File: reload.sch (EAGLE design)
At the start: 19 parts, among them IC3 OPAMP-DUALU, Q1 BTS117

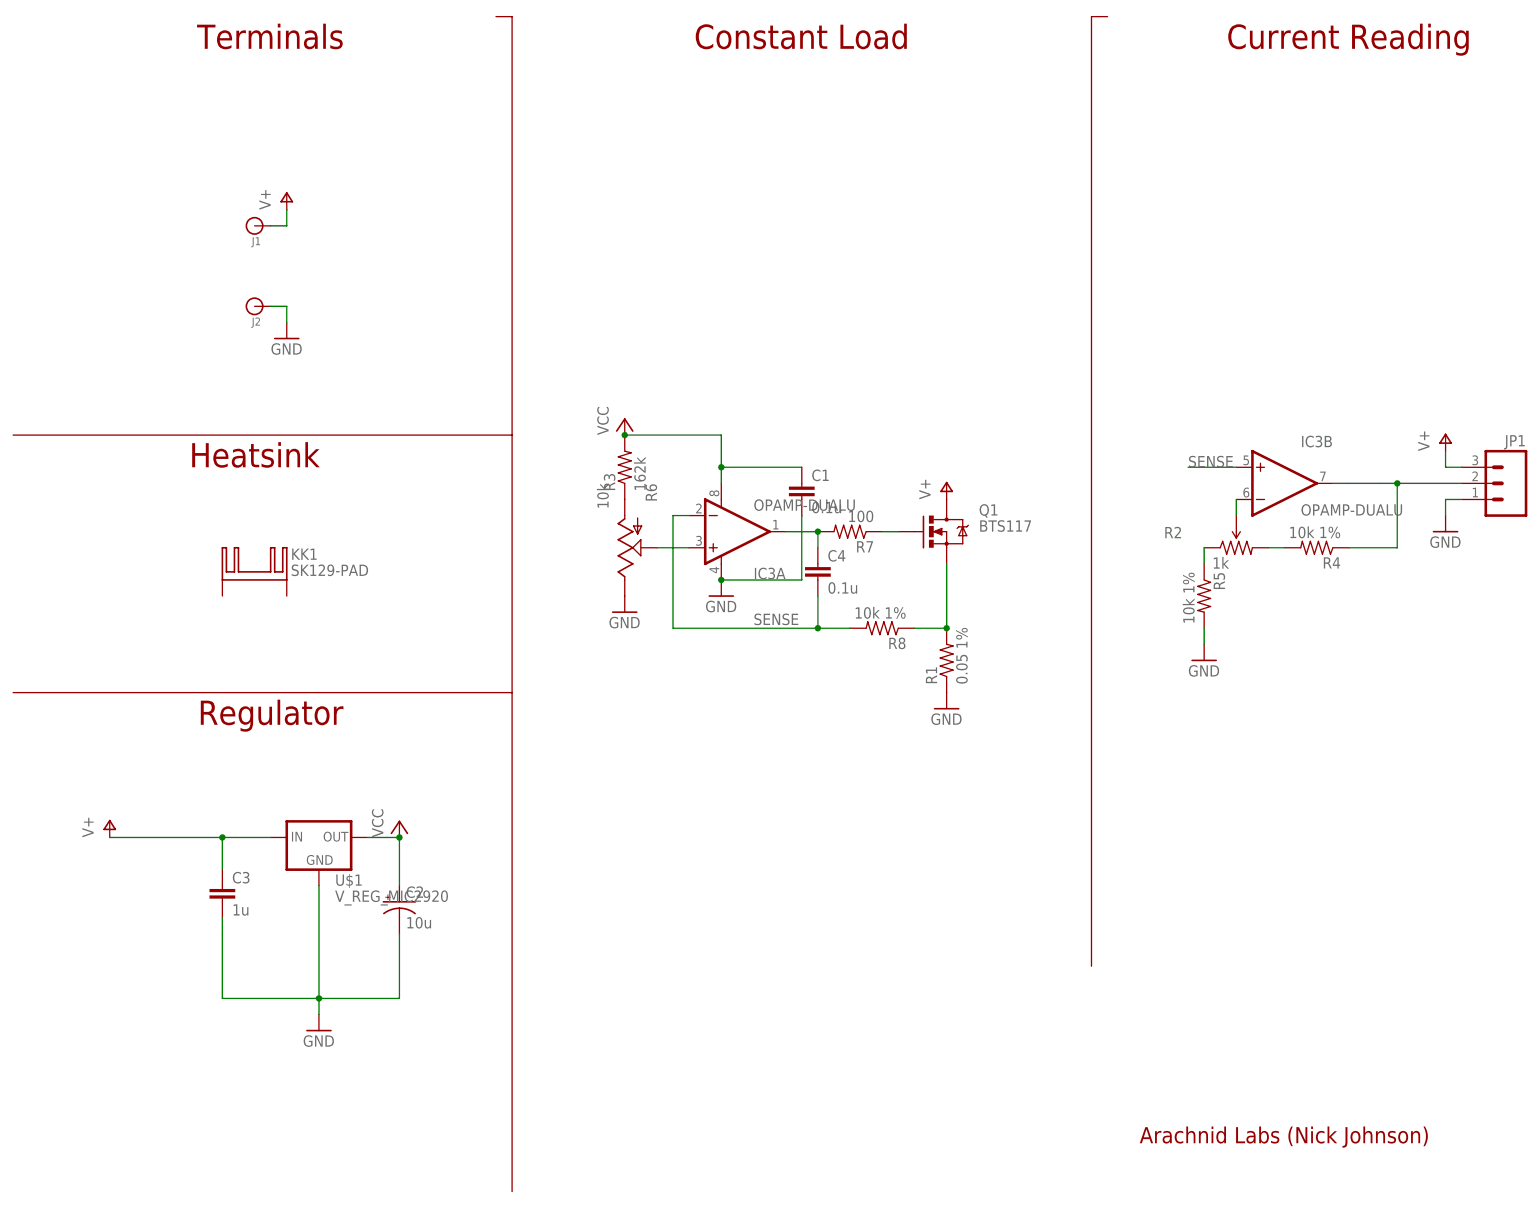
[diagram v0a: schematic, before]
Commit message: Respin with SMD parts
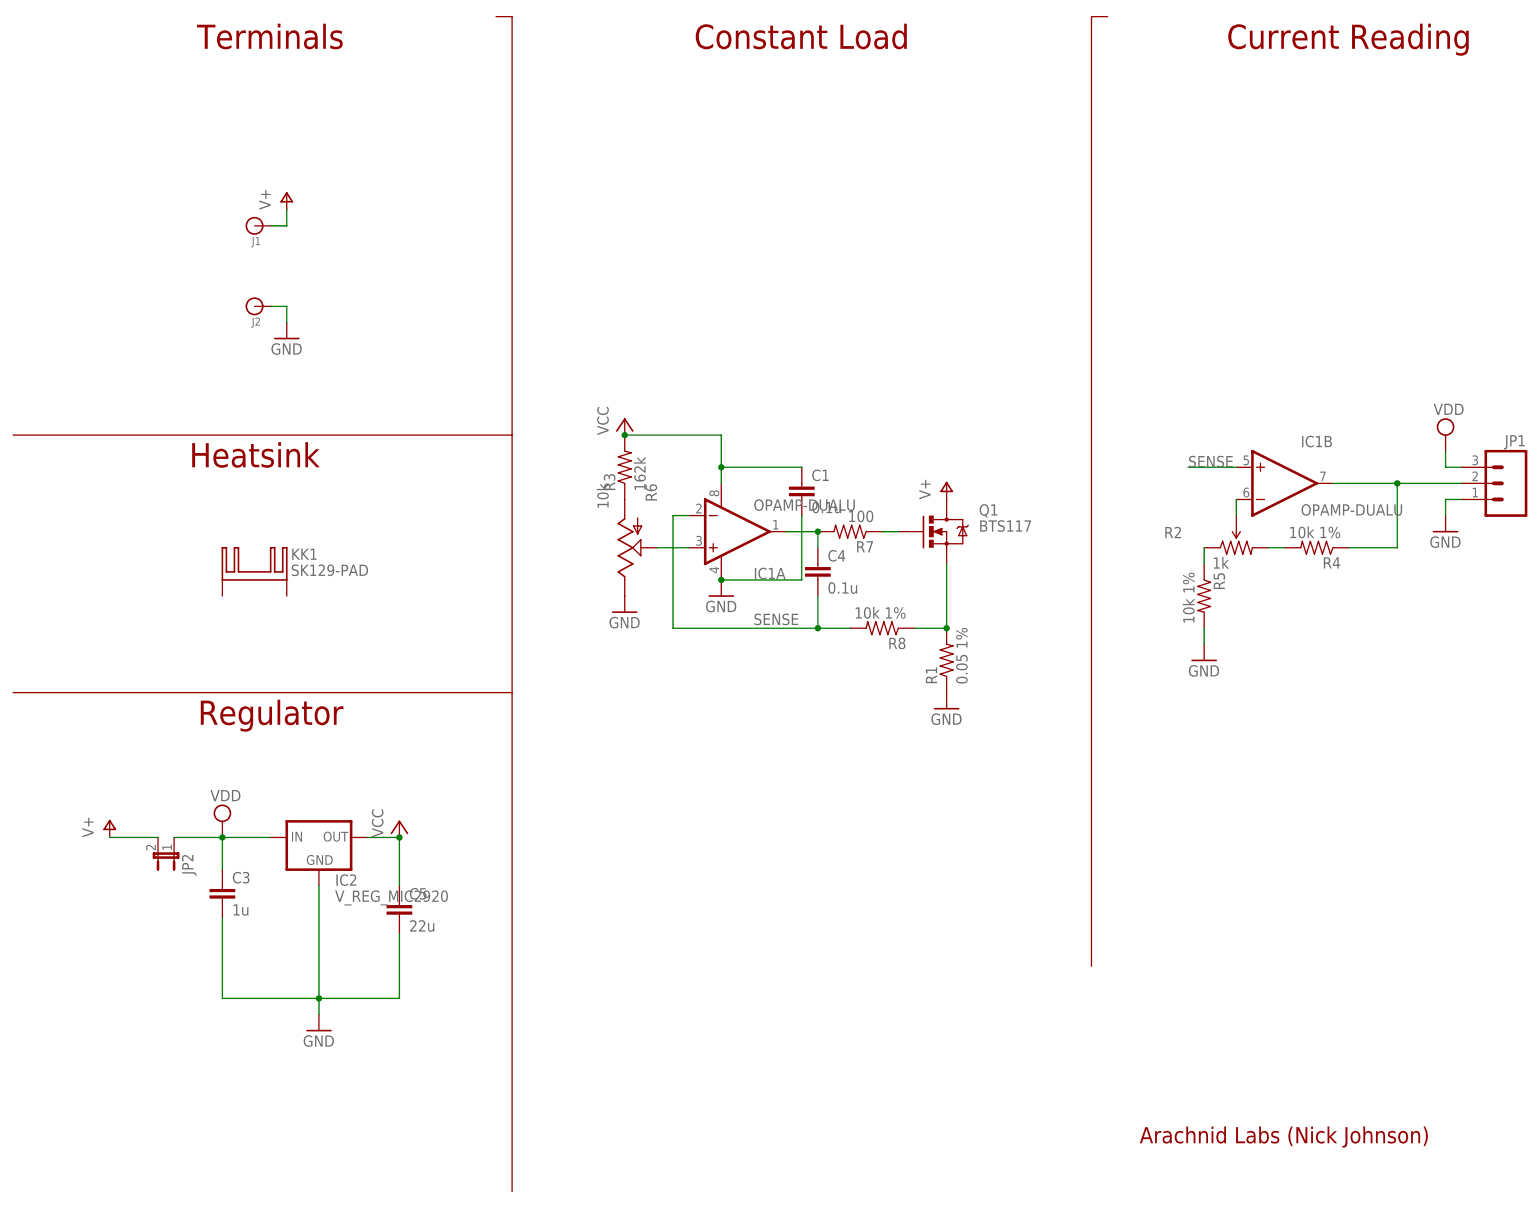
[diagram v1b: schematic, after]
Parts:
- removed C2: 10u, SparkFun-Passives:CAP_POLC
- added C5: 22u, SparkFun-Passives:CAP0805
- added JP2: (no value), SparkFun-Passives:JUMPER-2SMD-NC
- renumbered IC3 to IC1, U$1 to IC2
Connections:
- new net VDD: C3.1, IC2.IN, JP1.3, JP2.1
- net GND: now also C5.2; no longer C2.-
- net V+: now also JP2.2; no longer C3.1, IC2.IN, JP1.3
- net VCC: now also C5.1; no longer C2.+
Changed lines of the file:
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@@
 <?xml version="1.0" encoding="utf-8"?>
 <!DOCTYPE eagle SYSTEM "eagle.dtd">
-<eagle version="6.2">
+<eagle version="6.4">
 <drawing>
 <settings>
@@
 <part name="P+4" library="supply1" deviceset="V+" device=""/>
 <part name="GND7" library="supply1" deviceset="GND" device=""/>
-<part name="C2" library="SparkFun-Passives" deviceset="CAP_POL" device="C" value="10u"/>
 <part name="C3" library="SparkFun-Passives" deviceset="CAP" device="0805" value="1u"/>
 <part name="KK1" library="nickparts" deviceset="SK129-PAD" device=""/>
@@
 <part name="P+5" library="supply1" deviceset="VCC" device=""/>
 <part name="RELOAD" library="SparkFun-Aesthetics" deviceset="FRAME-LETTER" device=""/>
-<part name="IC3" library="SparkFun-AnalogIC" deviceset="OPAMP-DUAL" device="U"/>
-<part name="U$1" library="SparkFun-PowerIC" deviceset="V_REG_MIC2920" device=""/>
+<part name="IC1" library="SparkFun-AnalogIC" deviceset="OPAMP-DUAL" device="U"/>
+<part name="IC2" library="SparkFun-PowerIC" deviceset="V_REG_MIC2920" device=""/>
 <part name="JP1" library="SparkFun-Connectors" deviceset="M03" device="1X03_NO_SILK"/>
 <part name="R8" library="SparkFun-Passives" deviceset="RESISTOR" device="0805-RES" value="10k 1%"/>
 <part name="C4" library="SparkFun-Passives" deviceset="CAP" device="0805" value="0.1u"/>
-<part name="P+6" library="supply1" deviceset="V+" device=""/>
+<part name="JP2" library="SparkFun-Passives" deviceset="JUMPER-2" device="SMD-NC"/>
+<part name="SUPPLY1" library="supply2" deviceset="VDD" device=""/>
+<part name="SUPPLY2" library="supply2" deviceset="VDD" device=""/>
+<part name="C5" library="SparkFun-Passives" deviceset="CAP" device="0805" value="22u"/>
 </parts>
 <sheets>
@@
 <instance part="P+4" gate="1" x="43.18" y="157.48"/>
 <instance part="GND7" gate="1" x="43.18" y="134.62"/>
-<instance part="C2" gate="G$1" x="60.96" y="45.72"/>
 <instance part="C3" gate="G$1" x="33.02" y="45.72"/>
 <instance part="KK1" gate="G$1" x="38.1" y="96.52"/>
@@
 <instance part="RELOAD" gate="G$1" x="0" y="0"/>
 <instance part="RELOAD" gate="G$2" x="147.32" y="0"/>
-<instance part="IC3" gate="A" x="111.76" y="104.14"/>
-<instance part="IC3" gate="B" x="200.66" y="111.76"/>
-<instance part="U$1" gate="G$1" x="48.26" y="55.88"/>
+<instance part="IC1" gate="A" x="111.76" y="104.14"/>
+<instance part="IC1" gate="B" x="200.66" y="111.76"/>
+<instance part="IC2" gate="G$1" x="48.26" y="55.88"/>
 <instance part="JP1" gate="G$1" x="236.22" y="111.76" rot="MR0"/>
 <instance part="R8" gate="G$1" x="137.16" y="88.9" rot="R180"/>
 <instance part="C4" gate="G$1" x="127" y="96.52"/>
-<instance part="P+6" gate="1" x="226.06" y="119.38"/>
+<instance part="JP2" gate="A" x="25.4" y="53.34" rot="R180"/>
+<instance part="SUPPLY1" gate="G$1" x="33.02" y="58.42"/>
+<instance part="SUPPLY2" gate="G$1" x="226.06" y="119.38"/>
+<instance part="C5" gate="G$1" x="60.96" y="43.18"/>
 </instances>
 <busses>
@@
 </segment>
 <segment>
+<pinref part="JP2" gate="A" pin="2"/>
 <pinref part="P+3" gate="1" pin="V+"/>
-<wire x1="15.24" y1="55.88" x2="20.32" y2="55.88" width="0.1524" layer="91"/>
-<wire x1="25.4" y1="55.88" x2="27.94" y2="55.88" width="0.1524" layer="91"/>
-<wire x1="27.94" y1="55.88" x2="33.02" y2="55.88" width="0.1524" layer="91"/>
-<pinref part="C3" gate="G$1" pin="1"/>
-<wire x1="33.02" y1="55.88" x2="40.64" y2="55.88" width="0.1524" layer="91"/>
-<wire x1="33.02" y1="50.8" x2="33.02" y2="55.88" width="0.1524" layer="91"/>
-<junction x="33.02" y="55.88"/>
-<pinref part="U$1" gate="G$1" pin="IN"/>
-<wire x1="20.32" y1="55.88" x2="25.4" y2="55.88" width="0.1524" layer="91"/>
-</segment>
-<segment>
-<pinref part="JP1" gate="G$1" pin="3"/>
-<wire x1="228.6" y1="114.3" x2="226.06" y2="114.3" width="0.1524" layer="91"/>
-<wire x1="226.06" y1="114.3" x2="226.06" y2="116.84" width="0.1524" layer="91"/>
-<pinref part="P+6" gate="1" pin="V+"/>
+<wire x1="15.24" y1="55.88" x2="22.86" y2="55.88" width="0.1524" layer="91"/>
 </segment>
 </net>
@@
 <wire x1="193.04" y1="114.3" x2="185.42" y2="114.3" width="0.1524" layer="91"/>
 <label x="185.42" y="114.3" size="1.778" layer="95"/>
-<pinref part="IC3" gate="B" pin="+IN"/>
+<pinref part="IC1" gate="B" pin="+IN"/>
 </segment>
 <segment>
@@
 <wire x1="127" y1="88.9" x2="104.14" y2="88.9" width="0.1524" layer="91"/>
 <wire x1="104.14" y1="88.9" x2="104.14" y2="106.68" width="0.1524" layer="91"/>
-<pinref part="IC3" gate="A" pin="-IN"/>
+<pinref part="IC1" gate="A" pin="-IN"/>
 <wire x1="104.14" y1="106.68" x2="106.68" y2="106.68" width="0.1524" layer="91"/>
 <pinref part="C4" gate="G$1" pin="2"/>
@@
 <wire x1="124.46" y1="106.68" x2="124.46" y2="96.52" width="0.1524" layer="91"/>
 <wire x1="124.46" y1="96.52" x2="111.76" y2="96.52" width="0.1524" layer="91"/>
-<pinref part="IC3" gate="A" pin="V-"/>
+<pinref part="IC1" gate="A" pin="V-"/>
 <junction x="111.76" y="96.52"/>
 </segment>
@@
 <pinref part="GND4" gate="1" pin="GND"/>
 <wire x1="48.26" y1="27.94" x2="48.26" y2="30.48" width="0.1524" layer="91"/>
-<pinref part="C2" gate="G$1" pin="-"/>
 <wire x1="60.96" y1="40.64" x2="60.96" y2="30.48" width="0.1524" layer="91"/>
 <wire x1="60.96" y1="30.48" x2="48.26" y2="30.48" width="0.1524" layer="91"/>
 <wire x1="48.26" y1="30.48" x2="33.02" y2="30.48" width="0.1524" layer="91"/>
-<wire x1="33.02" y1="30.48" x2="33.02" y2="40.64" width="0.1524" layer="91"/>
+<wire x1="33.02" y1="30.48" x2="33.02" y2="43.18" width="0.1524" layer="91"/>
 <junction x="48.26" y="30.48"/>
 <pinref part="C3" gate="G$1" pin="2"/>
-<wire x1="33.02" y1="40.64" x2="33.02" y2="43.18" width="0.1524" layer="91"/>
 <wire x1="48.26" y1="48.26" x2="48.26" y2="30.48" width="0.1524" layer="91"/>
-<pinref part="U$1" gate="G$1" pin="GND"/>
+<pinref part="IC2" gate="G$1" pin="GND"/>
+<pinref part="C5" gate="G$1" pin="2"/>
 </segment>
 <segment>
@@
 <pinref part="R6" gate="G$1" pin="S"/>
 <wire x1="101.6" y1="101.6" x2="106.68" y2="101.6" width="0.1524" layer="91"/>
-<pinref part="IC3" gate="A" pin="+IN"/>
+<pinref part="IC1" gate="A" pin="+IN"/>
 </segment>
 </net>
@@
 <pinref part="R4" gate="G$1" pin="1"/>
 <wire x1="210.82" y1="101.6" x2="218.44" y2="101.6" width="0.1524" layer="91"/>
-<pinref part="IC3" gate="B" pin="OUT"/>
+<pinref part="IC1" gate="B" pin="OUT"/>
 <pinref part="JP1" gate="G$1" pin="2"/>
 <wire x1="228.6" y1="111.76" x2="218.44" y2="111.76" width="0.1524" layer="91"/>
@@
 <pinref part="R2" gate="R?" pin="WIPER"/>
 <wire x1="193.04" y1="109.22" x2="193.04" y2="106.68" width="0.1524" layer="91"/>
-<pinref part="IC3" gate="B" pin="-IN"/>
+<pinref part="IC1" gate="B" pin="-IN"/>
 </segment>
 </net>
@@
 <pinref part="R7" gate="G$1" pin="2"/>
 <wire x1="127" y1="104.14" x2="121.92" y2="104.14" width="0.1524" layer="91"/>
-<pinref part="IC3" gate="A" pin="OUT"/>
+<pinref part="IC1" gate="A" pin="OUT"/>
 <pinref part="C4" gate="G$1" pin="1"/>
 <wire x1="127" y1="104.14" x2="127" y2="101.6" width="0.1524" layer="91"/>
@@
 <pinref part="P+2" gate="VCC" pin="VCC"/>
 <wire x1="60.96" y1="48.26" x2="60.96" y2="55.88" width="0.1524" layer="91"/>
-<pinref part="C2" gate="G$1" pin="+"/>
-<pinref part="U$1" gate="G$1" pin="OUT"/>
+<pinref part="IC2" gate="G$1" pin="OUT"/>
+<pinref part="C5" gate="G$1" pin="1"/>
 </segment>
 <segment>
@@
 <junction x="111.76" y="114.3"/>
 <pinref part="P+5" gate="VCC" pin="VCC"/>
-<pinref part="IC3" gate="A" pin="V+"/>
+<pinref part="IC1" gate="A" pin="V+"/>
 </segment>
 </net>
@@
 </segment>
 </net>
+<net name="VDD" class="0">
+<segment>
+<wire x1="25.4" y1="55.88" x2="33.02" y2="55.88" width="0.1524" layer="91"/>
+<pinref part="C3" gate="G$1" pin="1"/>
+<wire x1="33.02" y1="55.88" x2="40.64" y2="55.88" width="0.1524" layer="91"/>
+<wire x1="33.02" y1="50.8" x2="33.02" y2="55.88" width="0.1524" layer="91"/>
+<junction x="33.02" y="55.88"/>
+<pinref part="IC2" gate="G$1" pin="IN"/>
+<pinref part="JP2" gate="A" pin="1"/>
+<pinref part="SUPPLY1" gate="G$1" pin="VDD"/>
+</segment>
+<segment>
+<pinref part="JP1" gate="G$1" pin="3"/>
+<wire x1="228.6" y1="114.3" x2="226.06" y2="114.3" width="0.1524" layer="91"/>
+<wire x1="226.06" y1="114.3" x2="226.06" y2="116.84" width="0.1524" layer="91"/>
+<pinref part="SUPPLY2" gate="G$1" pin="VDD"/>
+</segment>
+</net>

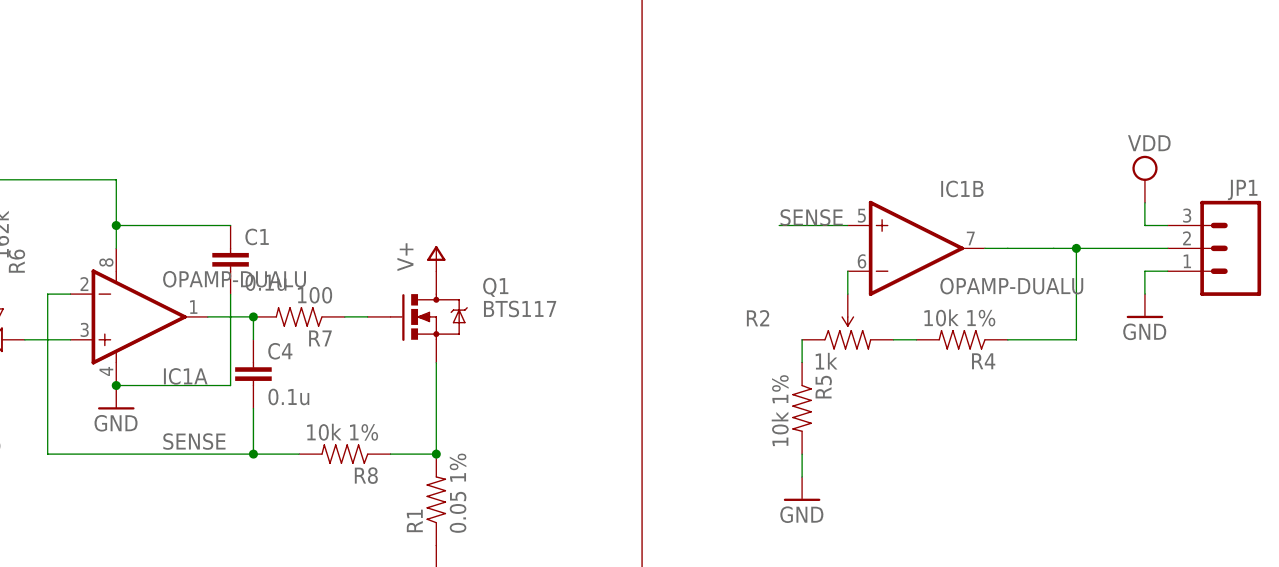
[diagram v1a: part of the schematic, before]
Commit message: Changes to SMD re:load v2; added test fixture
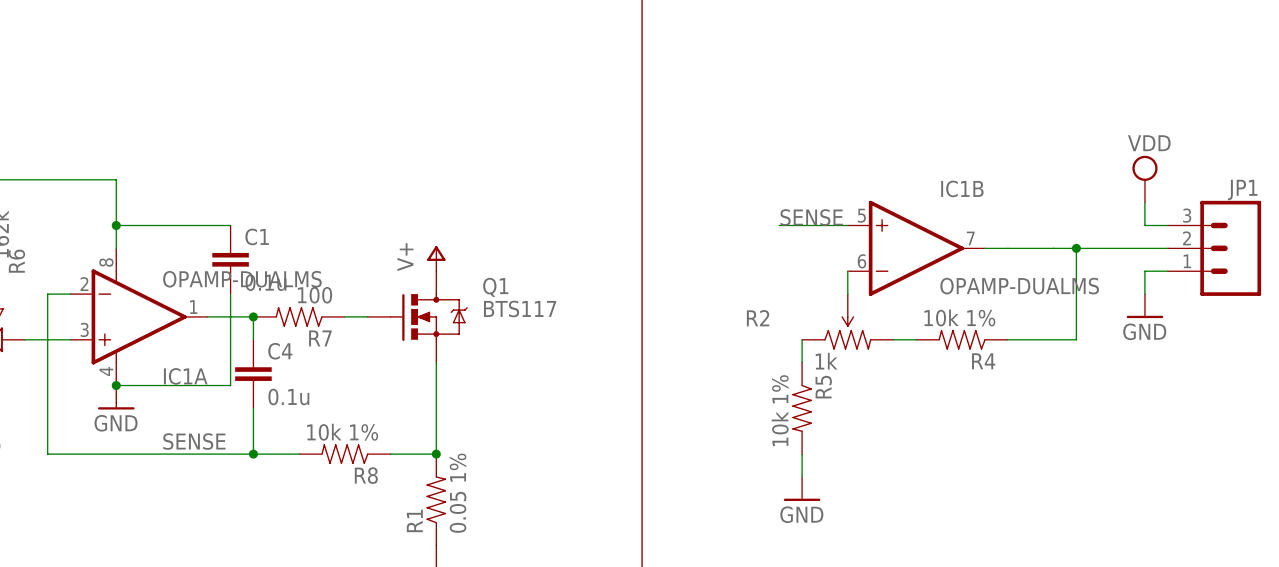
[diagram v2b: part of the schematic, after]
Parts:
- IC1: value OPAMP-DUALU -> OPAMP-DUALMS; device SparkFun-AnalogIC:OPAMP-DUALU -> nickparts:OPAMP-DUALMS
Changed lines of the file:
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@@
 <layer number="121" name="_tsilk" color="7" fill="1" visible="no" active="yes"/>
 <layer number="122" name="_bsilk" color="7" fill="1" visible="no" active="yes"/>
+<layer number="123" name="tTestmark" color="7" fill="1" visible="no" active="yes"/>
+<layer number="124" name="bTestmark" color="7" fill="1" visible="no" active="yes"/>
 <layer number="125" name="_tNames" color="7" fill="1" visible="no" active="yes"/>
 <layer number="126" name="_bNames" color="7" fill="1" visible="yes" active="yes"/>
 <layer number="127" name="_tValues" color="7" fill="1" visible="yes" active="yes"/>
 <layer number="128" name="_bValues" color="7" fill="1" visible="yes" active="yes"/>
+<layer number="131" name="tAdjust" color="7" fill="1" visible="no" active="yes"/>
+<layer number="132" name="bAdjust" color="7" fill="1" visible="no" active="yes"/>
 <layer number="144" name="Drill_legend" color="7" fill="1" visible="no" active="yes"/>
 <layer number="151" name="HeatSink" color="7" fill="1" visible="no" active="yes"/>
@@
 <part name="P+5" library="supply1" deviceset="VCC" device=""/>
 <part name="RELOAD" library="SparkFun-Aesthetics" deviceset="FRAME-LETTER" device=""/>
-<part name="IC1" library="SparkFun-AnalogIC" deviceset="OPAMP-DUAL" device="U"/>
+<part name="IC1" library="nickparts" deviceset="OPAMP-DUAL" device="MS"/>
 <part name="IC2" library="SparkFun-PowerIC" deviceset="V_REG_MIC2920" device=""/>
 <part name="JP1" library="SparkFun-Connectors" deviceset="M03" device="1X03_NO_SILK"/>
